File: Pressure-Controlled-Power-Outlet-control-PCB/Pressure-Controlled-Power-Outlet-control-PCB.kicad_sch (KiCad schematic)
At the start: 47 parts, among them J1 pressure sensor, J2 1017514, J3 I2C0 Connector, J4 SPI1 Connector, J5 FanA 5V/24V, J6 FanB 5V/24V, K1 T9GV5L24-24, K2 T9GV5L24-24, M1 Fan_4pin, M2 Fan_4pin, Q1 2N3906, Q2 IRF540N, Q3 IRF540N, Q4 2N3906, Q5 2N3904, Q6 2N3904, Q7 2N3904, Q8 2N3904, U1 Pico, U2 LM324, U3 LF50_TO220

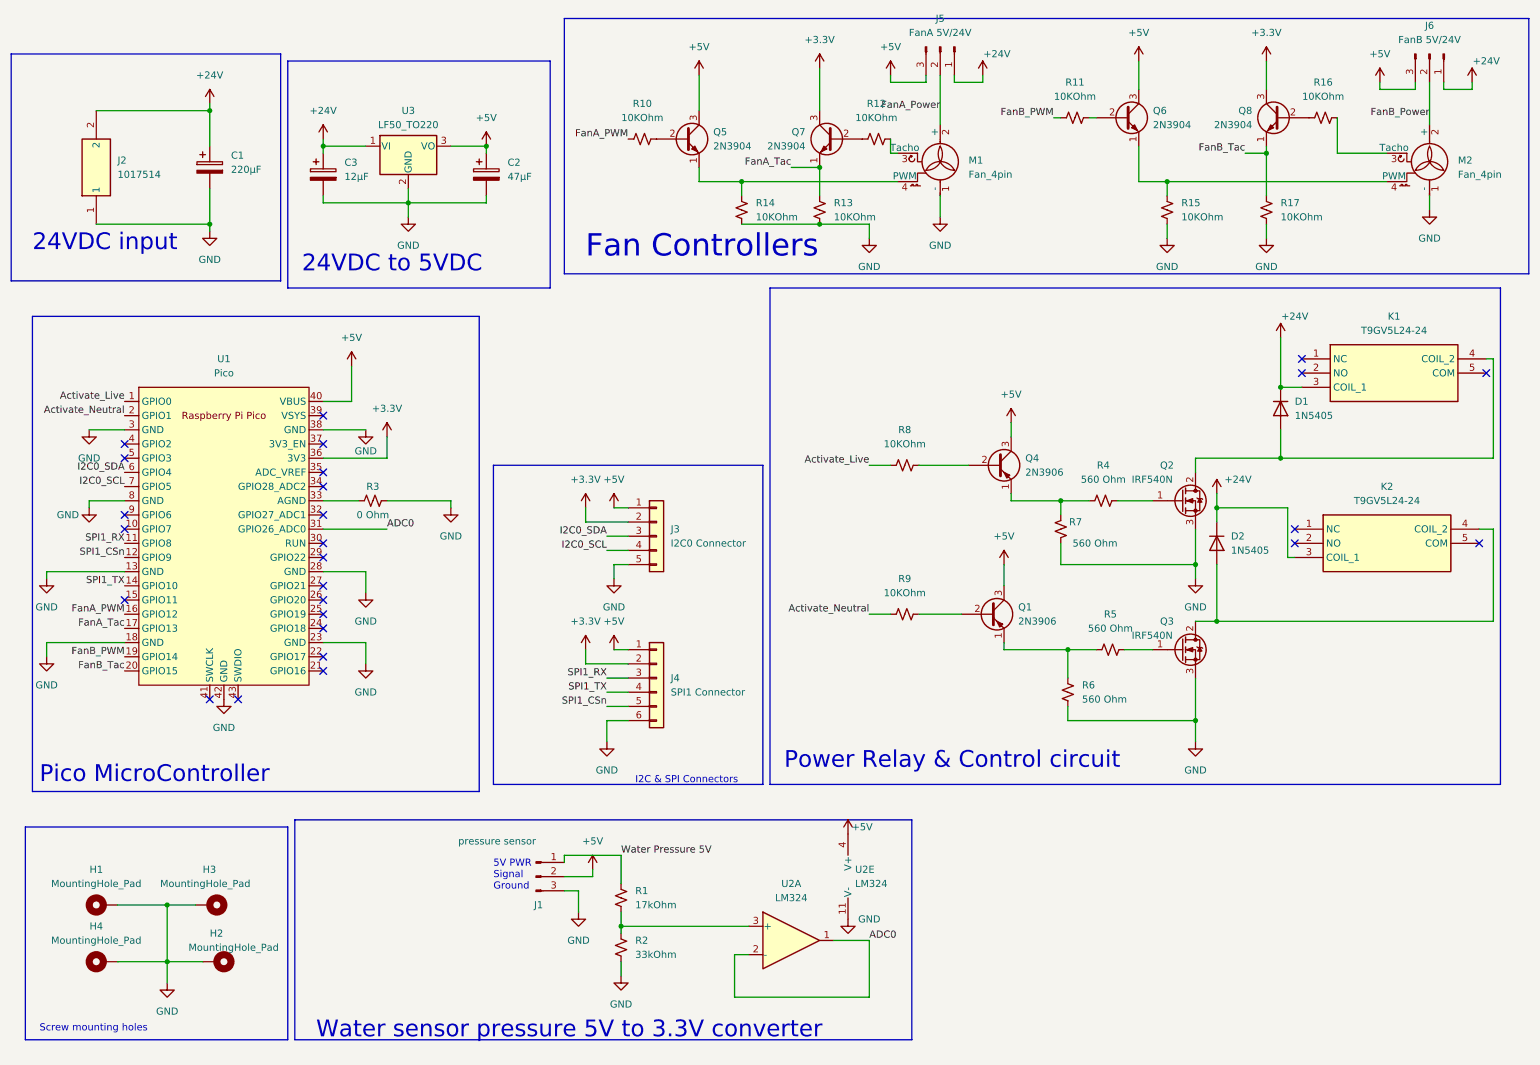
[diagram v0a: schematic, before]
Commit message: changed 24V fan power to 12V
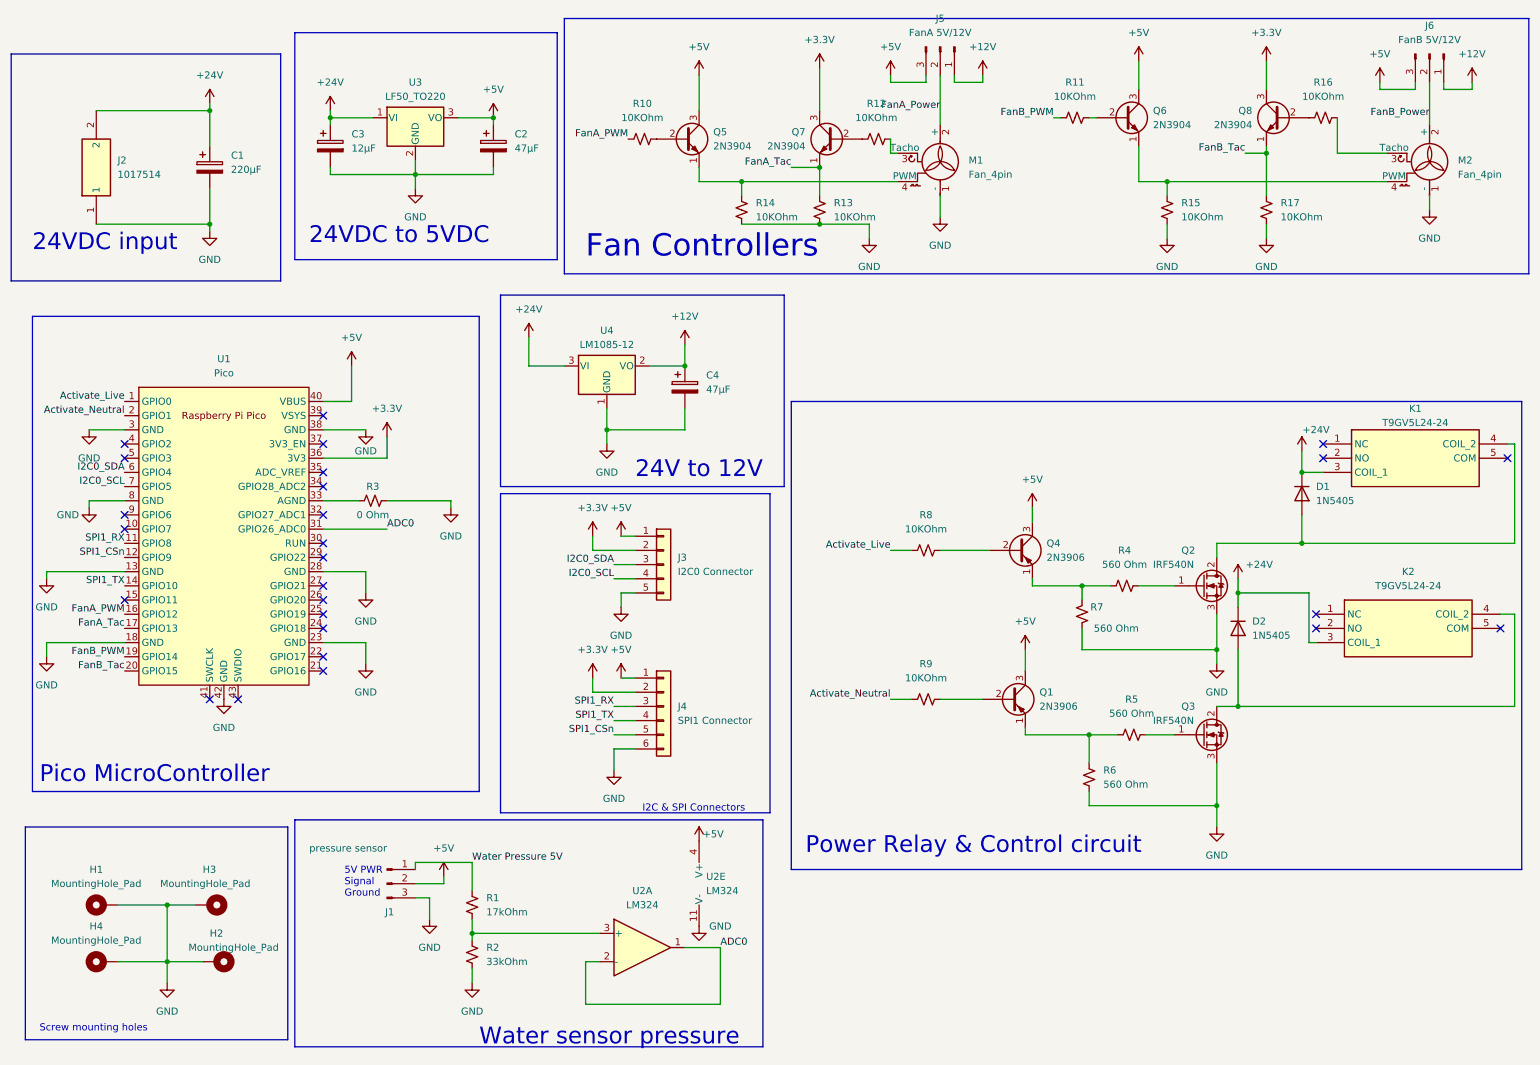
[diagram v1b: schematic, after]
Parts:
- added C4: 47µF, Capacitor_THT:CP_Radial_D10.0mm_P5.00mm, symbol Device:C_Polarized
- added U4: LM1085-12, Package_TO_SOT_THT:TO-220-3_Vertical, symbol Regulator_Linear:LM1085-12
- J5: value FanA 5V/24V -> FanA 5V/12V
- J6: value FanB 5V/24V -> FanB 5V/12V
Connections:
- net +24V: now also U4.3 (VI); no longer J5.1 (Pin_1), J6.1 (Pin_1)
- net GND: now also C4.2, U4.1 (GND)
- new net +12V: C4.1, J5.1 (Pin_1), J6.1 (Pin_1), U4.2 (VO)
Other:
- note added: "24V to 12V"
- note added: "Water sensor pressure"
- note removed: "Water sensor pressure 5V to 3.3V converter"
- moved on the sheet: C2, C3, D1, D2, J1, J3, J4, K1, K2, Q1, Q2, Q3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

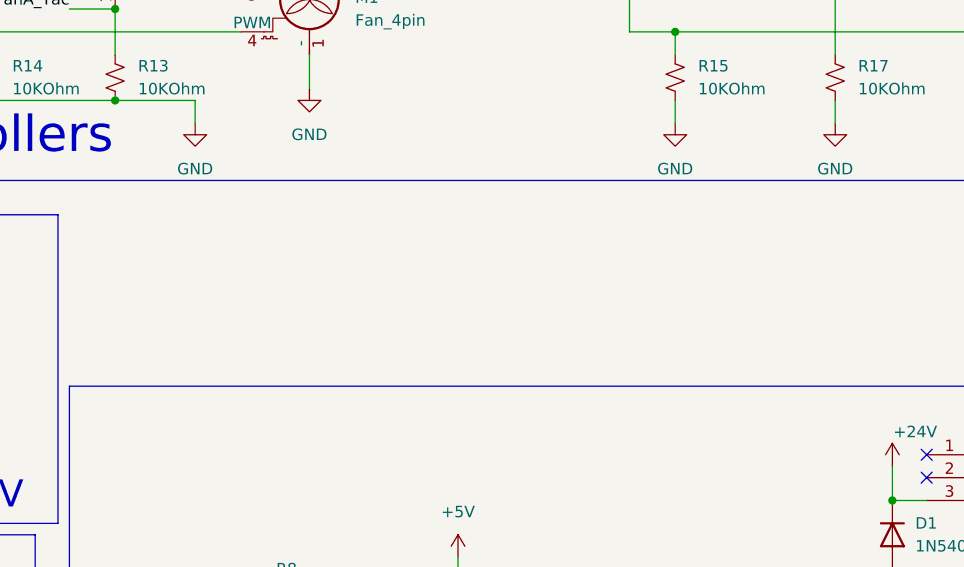
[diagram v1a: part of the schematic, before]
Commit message: added 5v fan headers
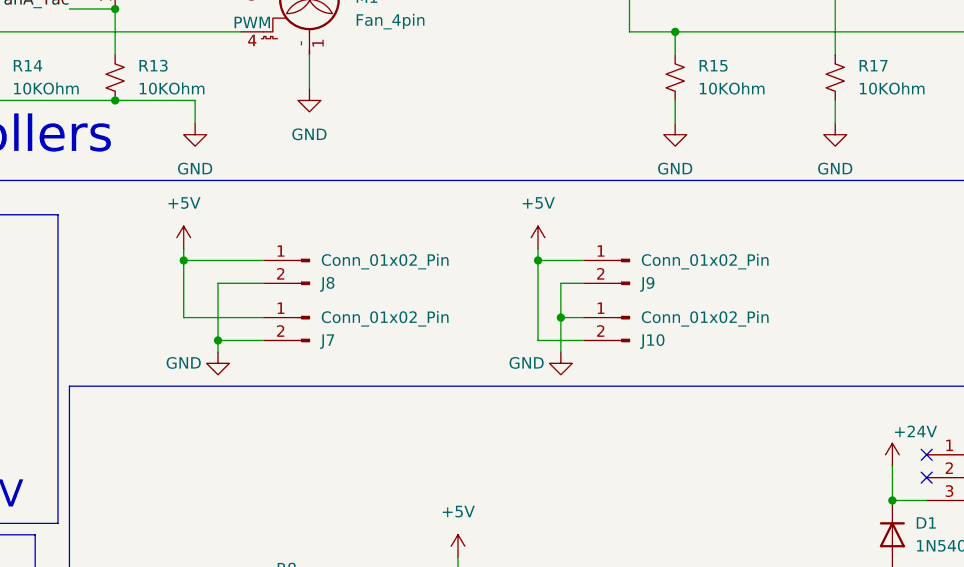
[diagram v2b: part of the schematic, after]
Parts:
- added J10, J9: Conn_01x02_Pin, Connector_PinHeader_2.54mm:PinHeader_1x02_P2.54mm_Vertical, symbol Connector:Conn_01x02_Pin
- added J7, J8: Conn_01x02_Pin, Connector_JST:JST_EH_B2B-EH-A_1x02_P2.50mm_Vertical, symbol Connector:Conn_01x02_Pin
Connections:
- net +5V: now also J10.2 (Pin_2), J7.1 (Pin_1), J8.1 (Pin_1), J9.1 (Pin_1)
- net GND: now also J10.1 (Pin_1), J7.2 (Pin_2), J8.2 (Pin_2), J9.2 (Pin_2)

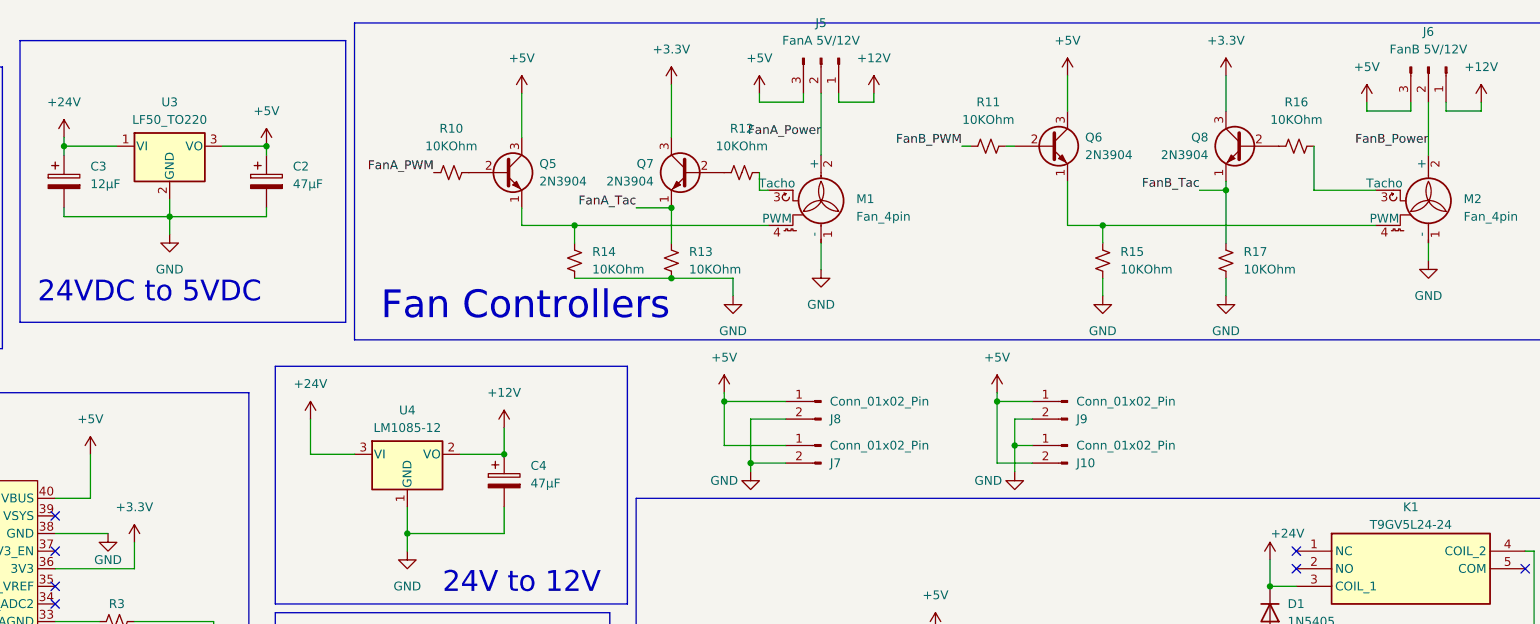
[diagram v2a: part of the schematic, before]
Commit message: added some basic diodes to protect from fan feedback
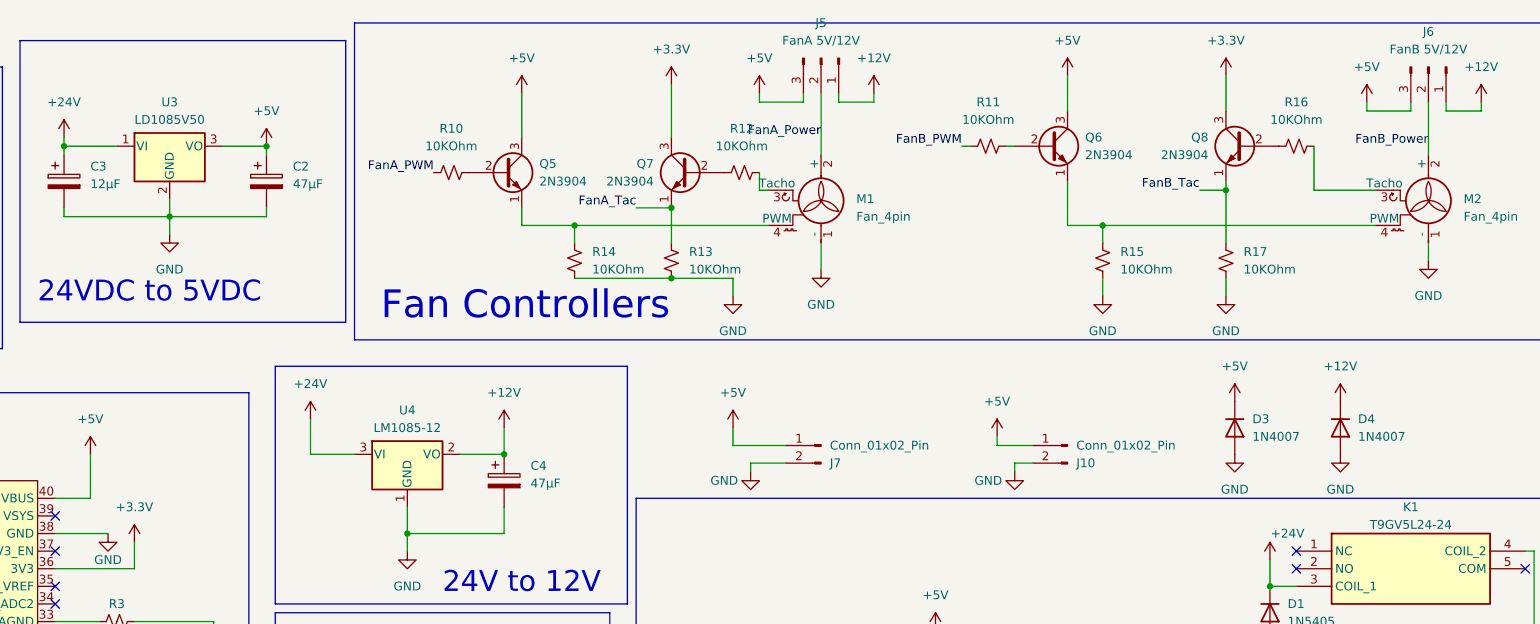
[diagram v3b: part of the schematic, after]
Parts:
- removed J8: Conn_01x02_Pin, Connector_JST:JST_EH_B2B-EH-A_1x02_P2.50mm_Vertical, symbol Connector:Conn_01x02_Pin
- removed J9: Conn_01x02_Pin, Connector_PinHeader_2.54mm:PinHeader_1x02_P2.54mm_Vertical, symbol Connector:Conn_01x02_Pin
- added D3, D4: 1N4007, Diode_THT:D_DO-41_SOD81_P10.16mm_Horizontal, symbol Diode:1N4007
- U3: value LF50_TO220 -> LD1085V50
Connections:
- net +12V: now also D4.1 (K)
- net +5V: now also J10.1 (Pin_1), D3.1 (K); no longer J10.2 (Pin_2)
- net GND: now also J10.2 (Pin_2), D3.2 (A), D4.2 (A); no longer J10.1 (Pin_1)
